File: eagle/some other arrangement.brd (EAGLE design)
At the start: 22 parts

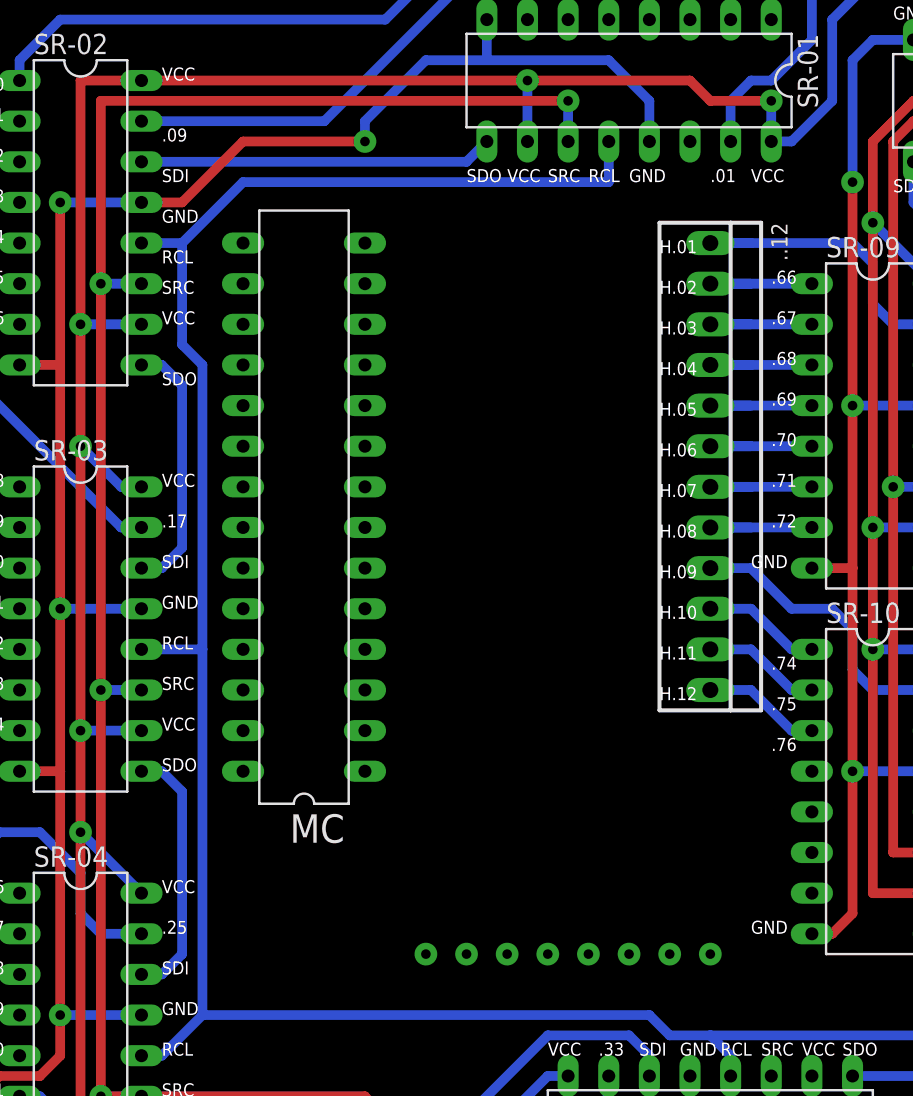
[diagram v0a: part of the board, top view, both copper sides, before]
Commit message: adaugat majoritatea componentelor + antentie la CHECKPOINT
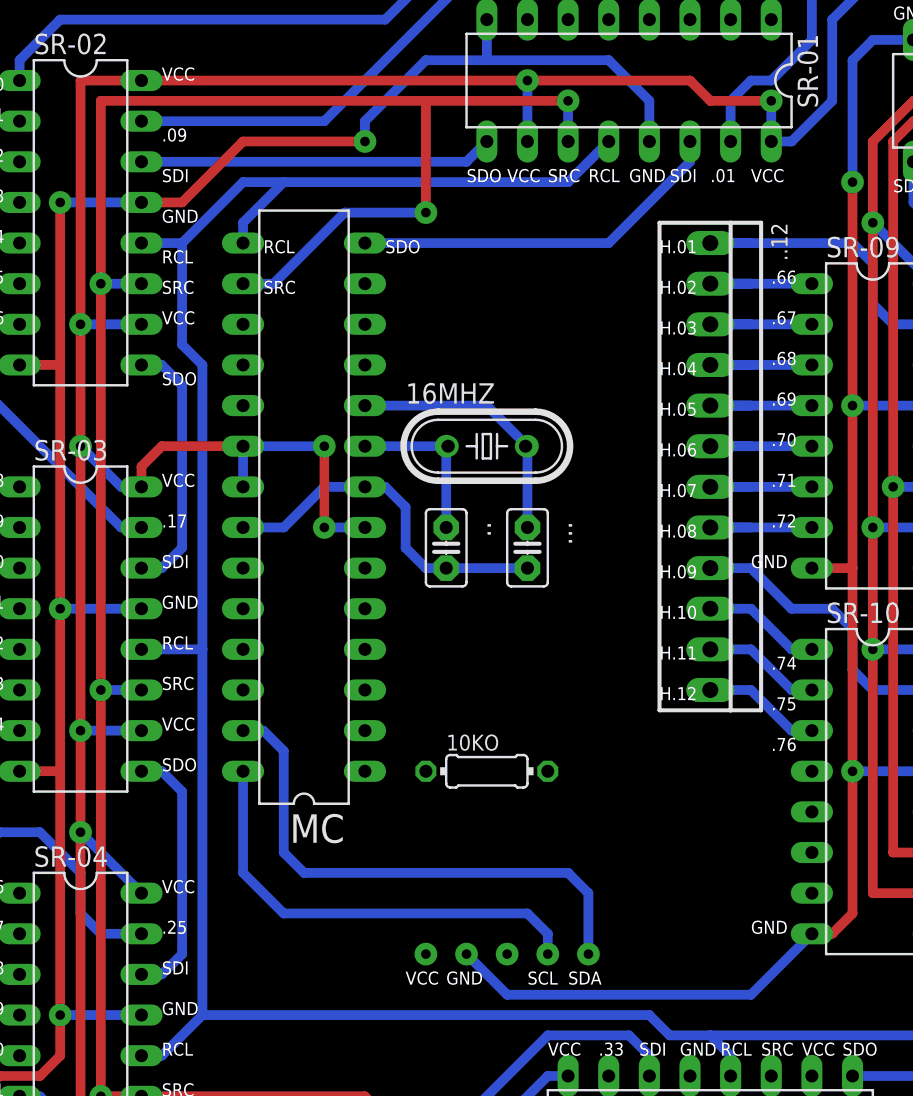
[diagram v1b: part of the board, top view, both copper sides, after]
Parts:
- added .., ...: 22 pF, capacitor-wima:C2.5-2
- added 10KO: (no value), resistor:0204/7
- added 16MHZ: (no value), crystal:HC49/S
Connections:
- removed net S$102: E$20.B, E$21.B, SR-03.8, SR-04.13, SR-04.8, SR-05.13, SR-05.8, SR-06.13, SR-06.8, SR-07.13, SR-07.8, SR-08.13, SR-08.8, SR-09.13, SR-09.8, SR-10.13, SR-10.8
- removed net S$95: E$18.B
- new net S$104: ...1, MC.9
- new net S$105: ....1, MC.10
- new net S$106: ....2, ...2, MC.22, MC.8
- new net S$107: E$18.B, E$20.B, E$21.B, MC.27, MC.28, SR-03.8, SR-04.13, SR-04.8, SR-05.13, SR-05.8, SR-06.13, SR-06.8, SR-07.13, SR-07.8, SR-08.13, SR-08.8, SR-09.13, SR-09.8, SR-10.13, SR-10.8
- new net S$108: MC.14, SR-01.14
- net S$49: now also MC.20, MC.21, MC.7
- net S$80: now also MC.15
- net S$81: now also MC.16
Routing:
- net S$107: track 0.00 -> 434.7 mm, vias 0 -> 17
- net S$102: track 341.5 -> 0.00 mm, vias 11 -> 0
- net S$108: track 0.00 -> 23.7 mm
- net S$49: track 406.9 -> 430.3 mm, vias 18 -> 20
- net S$106: track 0.00 -> 22.4 mm
- net S$81: track 302.4 -> 322.6 mm, vias 9 -> 10
- net S$105: track 0.00 -> 16.3 mm, vias 0 -> 1
- net S$104: track 0.00 -> 10.2 mm, vias 0 -> 1
- net S$95: track 7.40 -> 0.00 mm, vias 9 -> 0
- net S$80: track 218.7 -> 222.1 mm
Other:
- board text added: "SCL"
- board text added: "SDA"
